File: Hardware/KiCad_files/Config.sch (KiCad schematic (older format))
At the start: 19 parts, among them SW1 SW_Push, U1 XC7A25T_CSG325

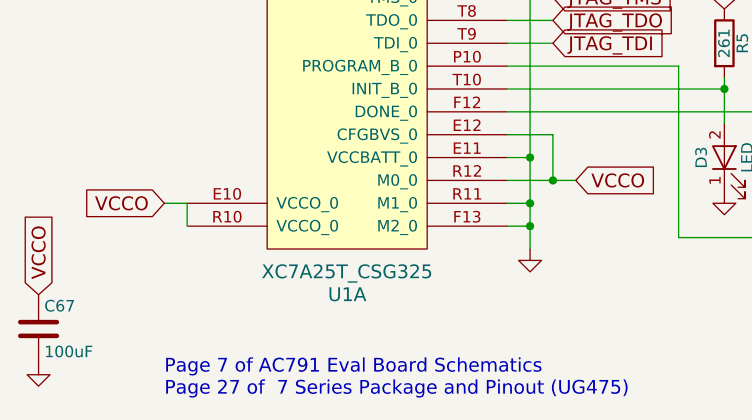
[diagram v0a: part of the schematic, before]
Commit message: Upgraded FPGA
Changed FPGA part from XC7A25T to XC7A35T
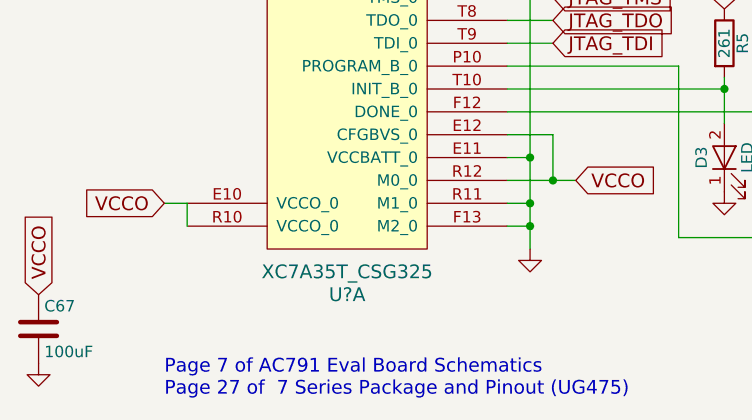
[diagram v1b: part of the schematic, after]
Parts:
- removed U1: XC7A25T_CSG325, symbol XC7A25T_CSG325
- added U?: XC7A35T_CSG325, symbol XC7A35T_CSG325
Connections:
- net CCLK: now also U?.E8 (CCLK_0)
- net GND: now also U?.E11 (VCCBATT_0), U?.F13 (M2_0), U?.J9 (GNDADC_0), U?.K10 (VP_0), U?.K9 (VREFN_0), U?.L10 (VREFP_0), U?.L9 (VN_0), U?.M10 (DXP_0), U?.M9 (DXN_0), U?.R11 (M1_0)
- net JTAG_TCK: now also U?.F8 (TCK_0)
- net JTAG_TDI: now also U?.T9 (TDI_0)
- net JTAG_TDO: now also U?.T8 (TDO_0)
- net JTAG_TMS: now also U?.R8 (TMS_0)
- net VCCAUX: now also U?.J10 (VCCADC_0)
- net VCCO: now also U?.E10 (VCCO_0), U?.E12 (CFGBVS_0), U?.R10 (VCCO_0), U?.R12 (M0_0)
- net at D4.2 (A), R6.2: now also U?.F12 (DONE_0)
- net at R7.2, SW1.1: now also U?.P10 (PROGRAM_B_0)
- net at D3.2 (A), R5.2: now also U?.T10 (INIT_B_0)
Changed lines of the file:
@@
 LIBS:valves
 LIBS:custom
-LIBS:pcie_test_1-cache
+LIBS:RASAC-cache
 EELAYER 25 0
 EELAYER END
@@
 Comment4 "The Cooper Union for the Advancement of Science and Art"
 $EndDescr
-$Comp
-L XC7A25T_CSG325 U1
-U 1 1 5C067A76
-P 3150 4600
-F 0 "U1" H 3150 4300 60  0000 C CNN
-F 1 "XC7A25T_CSG325" H 3150 4400 60  0000 C CNN
-F 2 "" H 3450 6350 60  0001 C CNN
-F 3 "" H 3450 6350 60  0001 C CNN
-	1    3150 4600
-	1    0    0    -1
-$EndComp
 Text GLabel 2350 4500 0    60   Input ~ 0
 VCCO
@@
 Wire Wire Line
 	7300 4600 7450 4600
+$Comp
+L XC7A35T_CSG325 U?
+U 1 1 5C174B0F
+P 3150 4600
+F 0 "U?" H 3150 4300 60  0000 C CNN
+F 1 "XC7A35T_CSG325" H 3150 4400 60  0000 C CNN
+F 2 "" H 3450 6350 60  0001 C CNN
+F 3 "" H 3450 6350 60  0001 C CNN
+	1    3150 4600
+	1    0    0    -1
+$EndComp
 $EndSCHEMATC

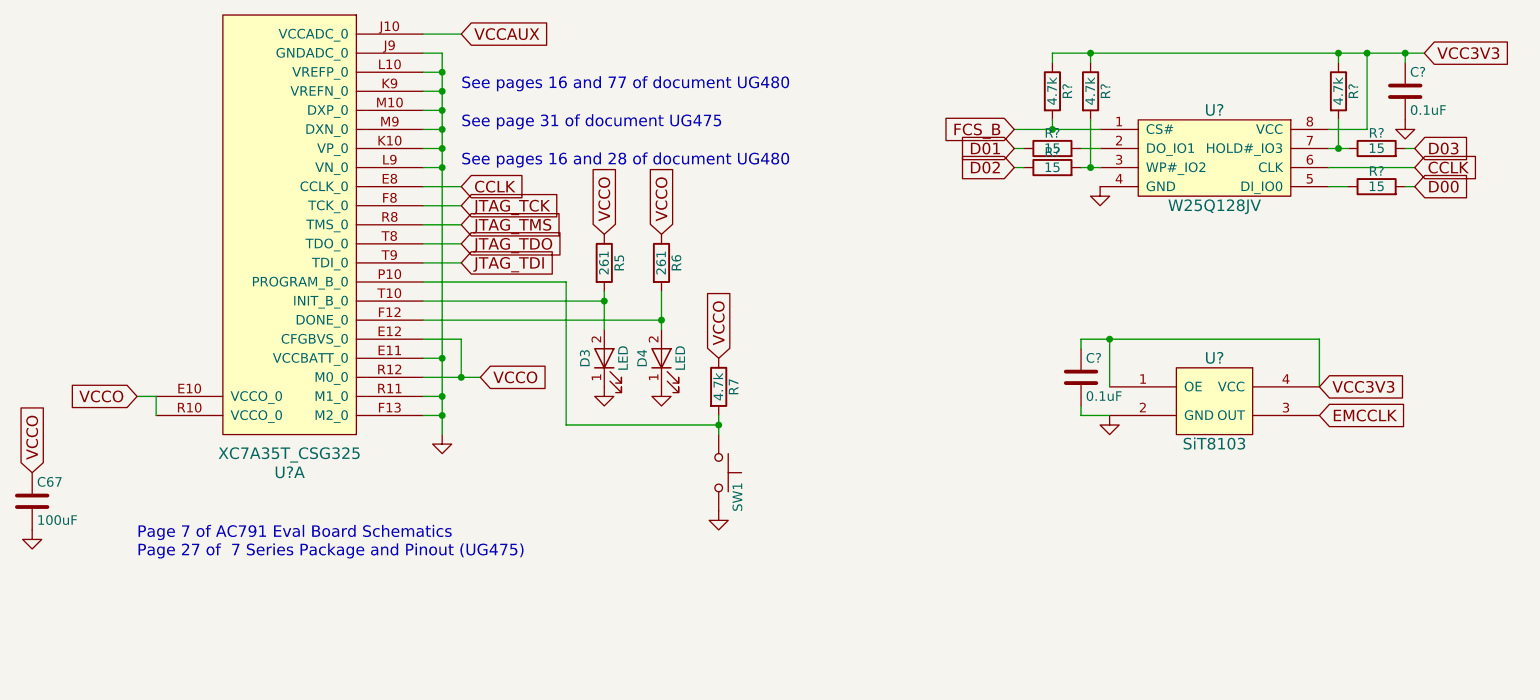
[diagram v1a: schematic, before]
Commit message: Added SYSCLK
Changed EMCCLK from SiT8103 to SiT8209 because Digikey didn't have.
Added SiT9102 200MHz for SYSCLK
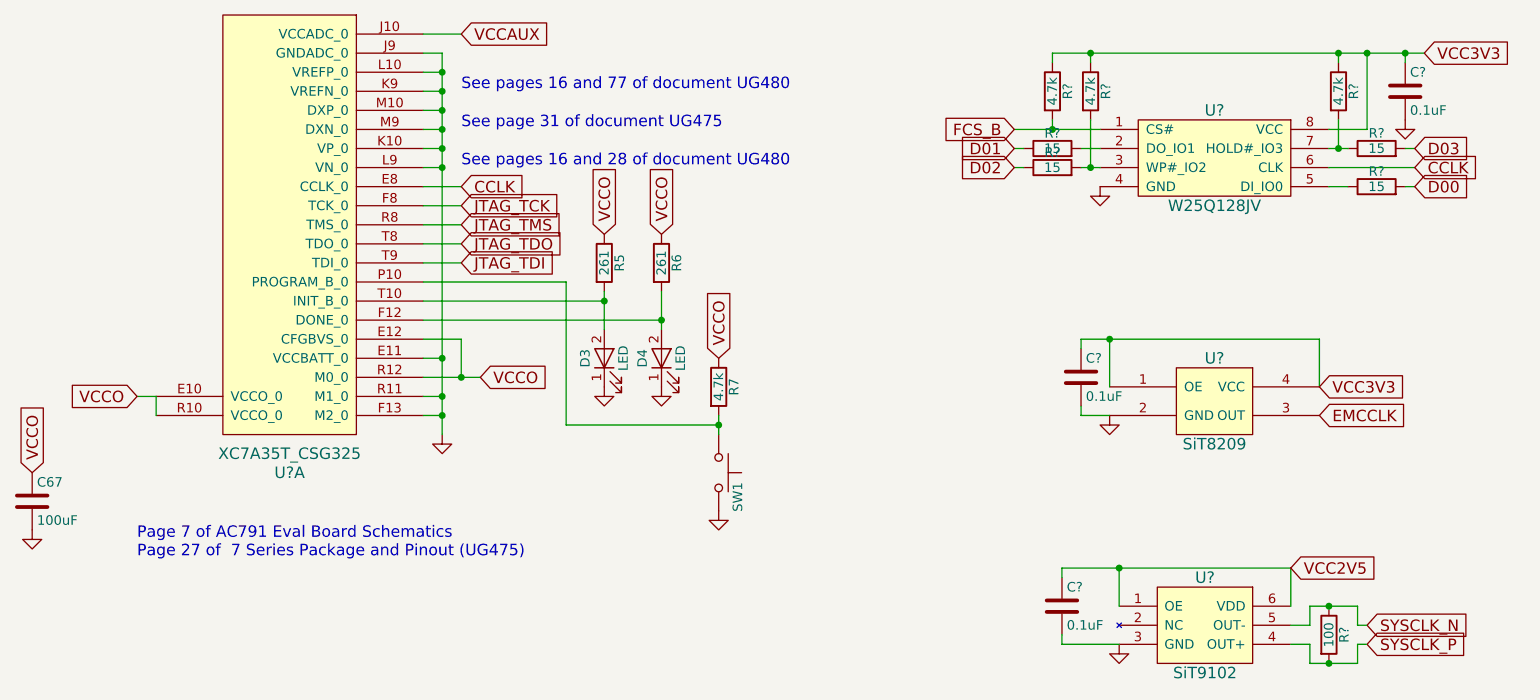
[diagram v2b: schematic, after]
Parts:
- removed U?: SiT8103, symbol SiT8103
- added C?: 0.1uF, symbol C
- added R?: 100, symbol R
- added U?: SiT8209, symbol SiT8209
- added U?: SiT9102, symbol SiT9102
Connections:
- net EMCCLK: now also U?.3 (OUT)
- net GND: now also C?.2, U?.2 (GND), U?.3 (GND)
- net VCC3V3: now also U?.1 (OE), U?.4 (VCC)
- new net SYSCLK_N: R?.1, U?.5 (OUT-)
- new net SYSCLK_P: R?.2, U?.4 (OUT+)
- new net VCC2V5: C?.1, U?.1 (OE), U?.6 (VDD)
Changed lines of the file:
@@
 	3950 4300 3850 4300
 Wire Wire Line
-	3950 2700 3950 4700
+	3950 2700 3950 2800
+Wire Wire Line
+	3950 2800 3950 2900
+Wire Wire Line
+	3950 2900 3950 3000
+Wire Wire Line
+	3950 3000 3950 3100
+Wire Wire Line
+	3950 3100 3950 3200
+Wire Wire Line
+	3950 3200 3950 3300
+Wire Wire Line
+	3950 3300 3950 4300
+Wire Wire Line
+	3950 4300 3950 4500
+Wire Wire Line
+	3950 4500 3950 4600
+Wire Wire Line
+	3950 4600 3950 4700
 Wire Wire Line
 	3850 2700 3950 2700
@@
 Connection ~ 3950 4600
 Wire Wire Line
-	3850 4400 4150 4400
+	3850 4400 4050 4400
+Wire Wire Line
+	4050 4400 4150 4400
 Wire Wire Line
 	3850 4200 4050 4200
@@
 Connection ~ 4050 4400
 Wire Wire Line
-	4800 3950 4800 4150
-Wire Wire Line
-	5100 3950 5100 4150
+	4800 3950 4800 4000
+Wire Wire Line
+	4800 4000 4800 4150
+Wire Wire Line
+	5100 3950 5100 4100
+Wire Wire Line
+	5100 4100 5100 4150
 Wire Wire Line
 	3850 4000 4800 4000
@@
 	4600 4650 5400 4650
 Wire Wire Line
-	5400 4600 5400 4700
+	5400 4600 5400 4650
+Wire Wire Line
+	5400 4650 5400 4700
 Connection ~ 5400 4650
 Wire Wire Line
@@
 Connection ~ 3950 3100
 Wire Wire Line
-	7150 2700 9100 2700
+	7150 2700 7350 2700
+Wire Wire Line
+	7350 2700 8650 2700
+Wire Wire Line
+	8650 2700 8800 2700
+Wire Wire Line
+	8800 2700 9000 2700
+Wire Wire Line
+	9000 2700 9100 2700
 $Comp
 L R R?
@@
 $EndComp
 Wire Wire Line
-	8600 3200 8700 3200
+	8600 3200 8650 3200
+Wire Wire Line
+	8650 3200 8700 3200
 Wire Wire Line
 	8600 3400 8700 3400
@@
 	7300 3200 7400 3200
 Wire Wire Line
-	7300 3300 7400 3300
+	7300 3300 7350 3300
+Wire Wire Line
+	7350 3300 7400 3300
 Wire Wire Line
 	8650 3200 8650 3050
@@
 FCS_B
 Wire Wire Line
-	6950 3100 7400 3100
+	6950 3100 7150 3100
+Wire Wire Line
+	7150 3100 7400 3100
 $Comp
 L R R?
@@
 	7150 3050 7150 3100
 Connection ~ 7150 3100
-$Comp
-L SiT8103 U?
-U 1 1 5C10AFD3
-P 8000 4550
-F 0 "U?" H 8000 4800 60  0000 C CNN
-F 1 "SiT8103" H 8000 4350 60  0000 C CNN
-F 2 "" H 7950 4550 60  0001 C CNN
-F 3 "" H 7950 4550 60  0001 C CNN
-	1    8000 4550
-	1    0    0    -1
-$EndComp
 Text GLabel 8550 4600 2    60   Input ~ 0
 EMCCLK
@@
 	8550 4200 8550 4450
 Wire Wire Line
-	7300 4200 8550 4200
+	7300 4200 7450 4200
+Wire Wire Line
+	7450 4200 8550 4200
 Wire Wire Line
 	7450 4200 7450 4450
@@
 	1    0    0    -1
 $EndComp
+$Comp
+L SiT8209 U?
+U 1 1 5C175774
+P 8000 4550
+F 0 "U?" H 8000 4800 60  0000 C CNN
+F 1 "SiT8209" H 8000 4350 60  0000 C CNN
+F 2 "" H 7950 4550 60  0001 C CNN
+F 3 "" H 7950 4550 60  0001 C CNN
+	1    8000 4550
+	1    0    0    -1
+$EndComp
+$Comp
+L SiT9102 U?
+U 1 1 5C176AC1
+P 7950 5700
+F 0 "U?" H 7950 5950 60  0000 C CNN
+F 1 "SiT9102" H 7950 5450 60  0000 C CNN
+F 2 "" H 7900 5700 60  0001 C CNN
+F 3 "" H 7900 5700 60  0001 C CNN
+	1    7950 5700
+	1    0    0    -1
+$EndComp
+Text GLabel 8400 5400 2    60   Input ~ 0
+VCC2V5
+$Comp
+L GND #PWR?
+U 1 1 5C176EFC
+P 7500 5800
+F 0 "#PWR?" H 7500 5550 50  0001 C CNN
+F 1 "GND" H 7500 5650 50  0001 C CNN
+F 2 "" H 7500 5800 50  0001 C CNN
+F 3 "" H 7500 5800 50  0001 C CNN
+	1    7500 5800
+	1    0    0    -1
+$EndComp
+$Comp
+L C C?
+U 1 1 5C176F02
+P 7200 5600
+F 0 "C?" H 7225 5700 50  0000 L CNN
+F 1 "0.1uF" H 7225 5500 50  0000 L CNN
+F 2 "" H 7238 5450 50  0001 C CNN
+F 3 "" H 7200 5600 50  0001 C CNN
+	1    7200 5600
+	1    0    0    -1
+$EndComp
+Wire Wire Line
+	7200 5800 7500 5800
+Wire Wire Line
+	7200 5400 7500 5400
+Wire Wire Line
+	7500 5400 8400 5400
+Wire Wire Line
+	8400 5400 8400 5600
+Wire Wire Line
+	7200 5800 7200 5750
+Wire Wire Line
+	7200 5450 7200 5400
+Wire Wire Line
+	7500 5600 7500 5400
+Connection ~ 7500 5400
+Text GLabel 8800 5700 2    60   Input ~ 0
+SYSCLK_N
+Text GLabel 8800 5800 2    60   Input ~ 0
+SYSCLK_P
+Wire Wire Line
+	8400 5700 8500 5700
+Wire Wire Line
+	8500 5700 8500 5600
+Wire Wire Line
+	8500 5600 8600 5600
+Wire Wire Line
+	8600 5600 8750 5600
+$Comp
+L R R?
+U 1 1 5C177A55
+P 8600 5750
+F 0 "R?" V 8680 5750 50  0000 C CNN
+F 1 "100" V 8600 5750 50  0000 C CNN
+F 2 "" V 8530 5750 50  0001 C CNN
+F 3 "" H 8600 5750 50  0001 C CNN
+	1    8600 5750
+	1    0    0    -1
+$EndComp
+Wire Wire Line
+	8400 5800 8500 5800
+Wire Wire Line
+	8500 5800 8500 5900
+Wire Wire Line
+	8500 5900 8600 5900
+Wire Wire Line
+	8600 5900 8750 5900
+Wire Wire Line
+	8750 5600 8750 5700
+Wire Wire Line
+	8750 5700 8800 5700
+Connection ~ 8600 5600
+Wire Wire Line
+	8750 5900 8750 5800
+Wire Wire Line
+	8750 5800 8800 5800
+Connection ~ 8600 5900
 $EndSCHEMATC

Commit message: Added  HDMI transmitter chip
Also added resistors and moved HDMI data pins around on FPGA side
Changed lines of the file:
@@
 	3950 4300 3850 4300
 Wire Wire Line
-	3950 2700 3950 2800
-Wire Wire Line
-	3950 2800 3950 2900
-Wire Wire Line
-	3950 2900 3950 3000
-Wire Wire Line
-	3950 3000 3950 3100
-Wire Wire Line
-	3950 3100 3950 3200
-Wire Wire Line
-	3950 3200 3950 3300
-Wire Wire Line
-	3950 3300 3950 4300
-Wire Wire Line
-	3950 4300 3950 4500
-Wire Wire Line
-	3950 4500 3950 4600
-Wire Wire Line
-	3950 4600 3950 4700
+	3950 2700 3950 4700
 Wire Wire Line
 	3850 2700 3950 2700
@@
 Connection ~ 3950 4600
 Wire Wire Line
-	3850 4400 4050 4400
-Wire Wire Line
-	4050 4400 4150 4400
+	3850 4400 4150 4400
 Wire Wire Line
 	3850 4200 4050 4200
@@
 Connection ~ 4050 4400
 Wire Wire Line
-	4800 3950 4800 4000
-Wire Wire Line
-	4800 4000 4800 4150
-Wire Wire Line
-	5100 3950 5100 4100
-Wire Wire Line
-	5100 4100 5100 4150
+	4800 3950 4800 4150
+Wire Wire Line
+	5100 3950 5100 4150
 Wire Wire Line
 	3850 4000 4800 4000
@@
 	4600 4650 5400 4650
 Wire Wire Line
-	5400 4600 5400 4650
-Wire Wire Line
-	5400 4650 5400 4700
+	5400 4600 5400 4700
 Connection ~ 5400 4650
 Wire Wire Line
@@
 Connection ~ 3950 3100
 Wire Wire Line
-	7150 2700 7350 2700
-Wire Wire Line
-	7350 2700 8650 2700
-Wire Wire Line
-	8650 2700 8800 2700
-Wire Wire Line
-	8800 2700 9000 2700
-Wire Wire Line
-	9000 2700 9100 2700
+	7150 2700 9100 2700
 $Comp
 L R R?
@@
 $EndComp
 Wire Wire Line
-	8600 3200 8650 3200
-Wire Wire Line
-	8650 3200 8700 3200
+	8600 3200 8700 3200
 Wire Wire Line
 	8600 3400 8700 3400
@@
 	7300 3200 7400 3200
 Wire Wire Line
-	7300 3300 7350 3300
-Wire Wire Line
-	7350 3300 7400 3300
+	7300 3300 7400 3300
 Wire Wire Line
 	8650 3200 8650 3050
@@
 FCS_B
 Wire Wire Line
-	6950 3100 7150 3100
-Wire Wire Line
-	7150 3100 7400 3100
+	6950 3100 7400 3100
 $Comp
 L R R?
@@
 	8550 4200 8550 4450
 Wire Wire Line
-	7300 4200 7450 4200
-Wire Wire Line
-	7450 4200 8550 4200
+	7300 4200 8550 4200
 Wire Wire Line
 	7450 4200 7450 4450
@@
 	7200 5800 7500 5800
 Wire Wire Line
-	7200 5400 7500 5400
-Wire Wire Line
-	7500 5400 8400 5400
+	7200 5400 8400 5400
 Wire Wire Line
 	8400 5400 8400 5600
@@
 	8500 5700 8500 5600
 Wire Wire Line
-	8500 5600 8600 5600
-Wire Wire Line
-	8600 5600 8750 5600
+	8500 5600 8750 5600
 $Comp
 L R R?
@@
 	8500 5800 8500 5900
 Wire Wire Line
-	8500 5900 8600 5900
-Wire Wire Line
-	8600 5900 8750 5900
+	8500 5900 8750 5900
 Wire Wire Line
 	8750 5600 8750 5700
